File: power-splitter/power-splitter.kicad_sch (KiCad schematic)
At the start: 17 parts, among them J1 Barrel_Jack, J2 USB_B_Micro, J3 Conn_01x02_Pin, J4 Conn_01x02_Pin, J5 Conn_02x02_Counter_Clockwise, SW1 SW_SP3T, U1 LM2594M-3.3

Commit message: Updated Rev Number
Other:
- title: (none) -> Power Splitter
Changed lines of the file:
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@@
   (paper "A4")
   (title_block
-    (date "2023-04-05")
-    (rev "0.1")
+    (title "Power Splitter")
+    (date "2023-04-11")
+    (rev "1.0")
   )
   (junction (at 247.396 52.832) (diameter 0) (color 0 0 0 0)

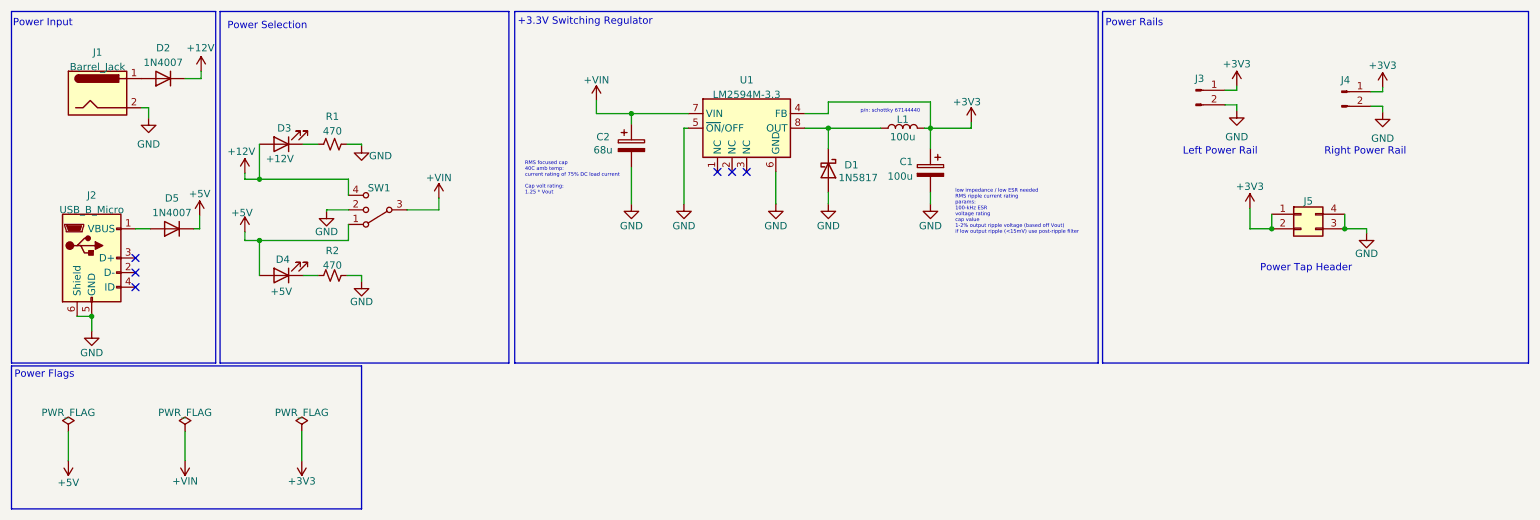
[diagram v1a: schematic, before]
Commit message: Updated schem/layout
+ Adjusted pours to filet edges
+ Added text for +3V3 outputs
+ Adjusted board edges to be less weird
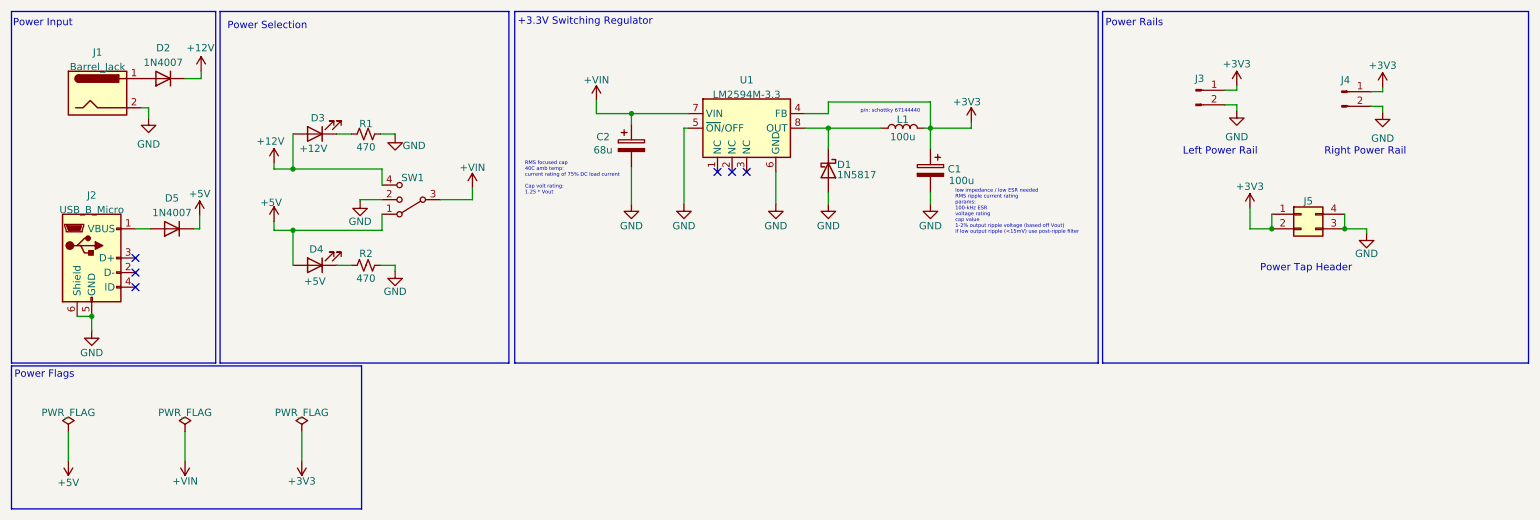
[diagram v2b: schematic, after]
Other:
- moved on the sheet: D3, D4, R1, R2, SW1

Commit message: Updated to Rev B
+ Adjusted layout to be more compact and to fit on 51mm wide breadboards
+ Added 3D STEP files for the barrel jack, USB-Micro B receptacle
+ Added PDFs for the schematic and top/bottom layer of the PCB
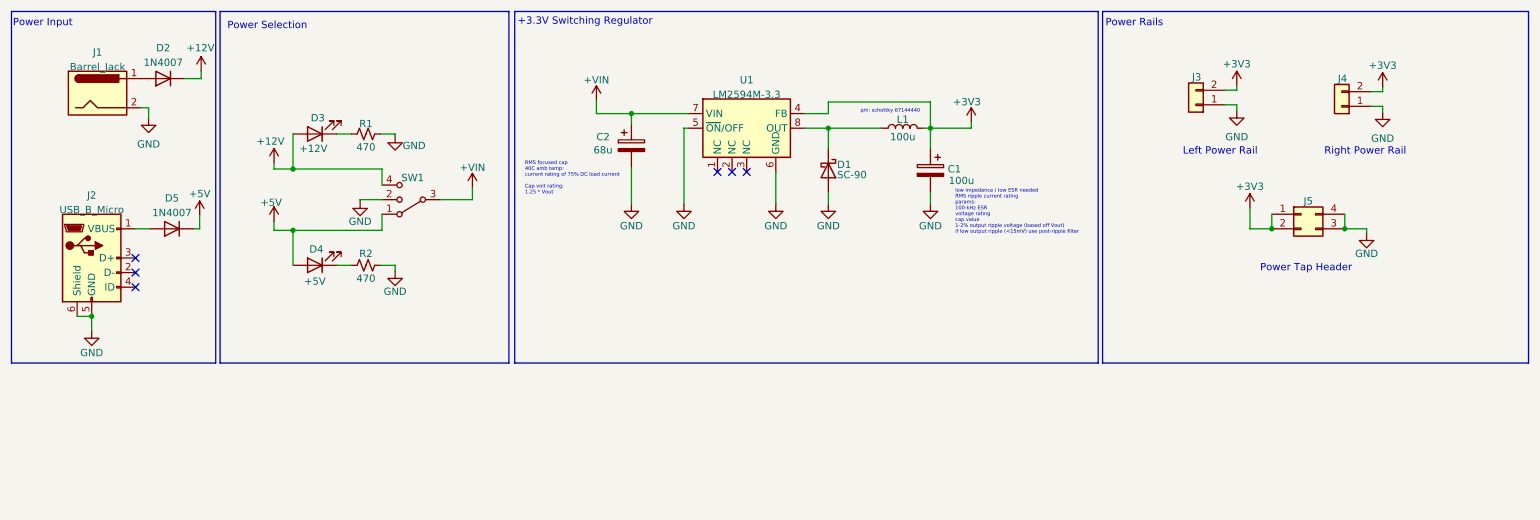
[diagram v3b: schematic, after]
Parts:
- removed J3, J4: Conn_01x02_Pin, Connector_PinHeader_2.00mm:PinHeader_1x02_P2.00mm_Vertical, symbol Connector:Conn_01x02_Pin
- added J3, J4: Conn_01x02, Connector_PinHeader_1.00mm:PinHeader_1x02_P1.00mm_Vertical, symbol Connector_Generic:Conn_01x02
- D1: value 1N5817 -> SC-90; footprint Diode_THT:D_DO-41_SOD81_P10.16mm_Horizontal -> Diode_SMD:D_SOD-323F
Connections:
- net +3V3: now also L1.1, J3.2 (Pin_2), J4.2 (Pin_2); no longer L1.2
- net GND: now also J3.1 (Pin_1), J4.1 (Pin_1)
- net at D1.1 (K), U1.8 (OUT): now also L1.2; no longer L1.1
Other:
- note removed: "Power Flags"
- moved on the sheet: L1
